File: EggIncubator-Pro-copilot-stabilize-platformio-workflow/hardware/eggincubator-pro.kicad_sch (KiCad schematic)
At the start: 33 parts, among them J1 ESP32 DevKit breakout, J10 ESP32 DevKit 5V / VIN input, J2 SHT31 module, I2C 0x44, J3 DS18B20, 1-Wire, J4 4 optocoupled relay-control o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, J5 BTS7960 module / motor (separ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, J6 Door and turner limit switches, J7 5V buzzer module, Q1 low-side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, J8 Expansion: I2C / ADC sensors, J9 12V DC input, Q1 PN2222A, U1 PC817, U2 PC817, U3 PC817, U4 PC817, U9 12V to 5V buck module

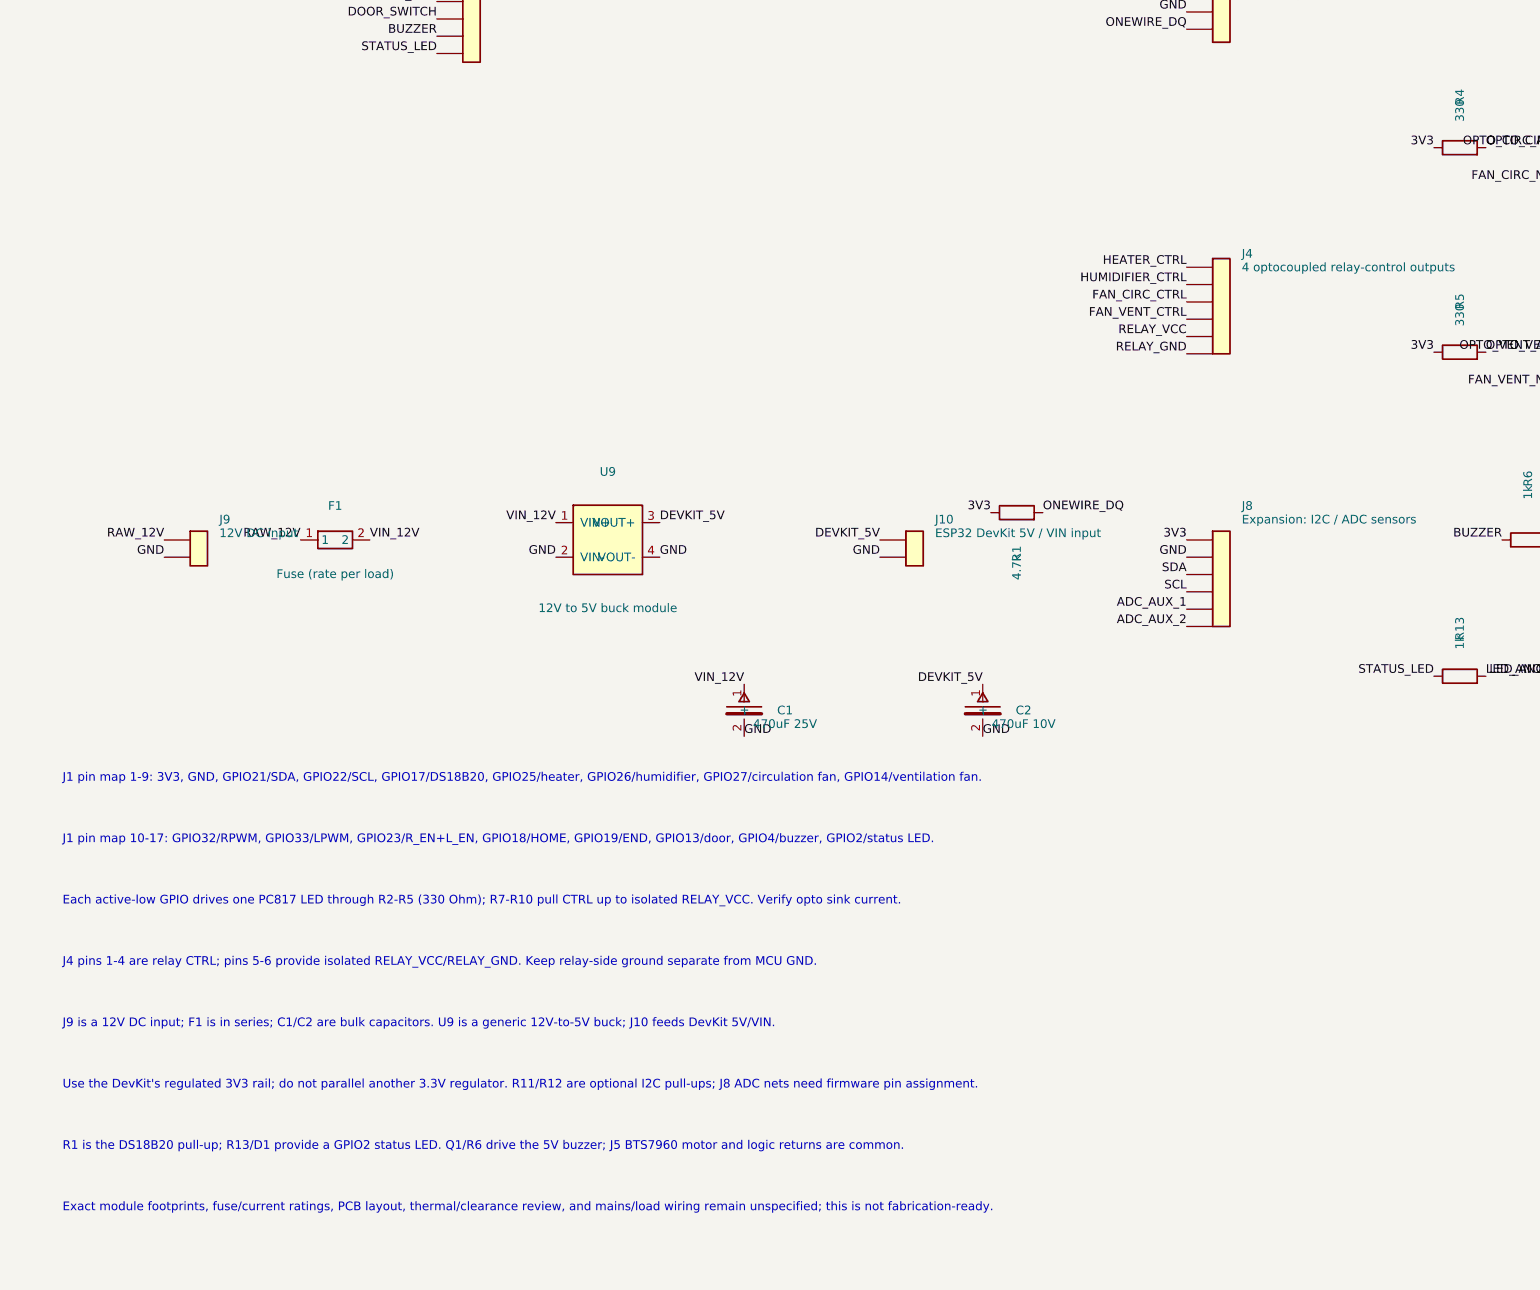
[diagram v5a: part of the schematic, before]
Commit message: Add fused motor power to schematic
Co-authored-by: tomnyle <175001228+tomnyle@users.noreply.github.com>
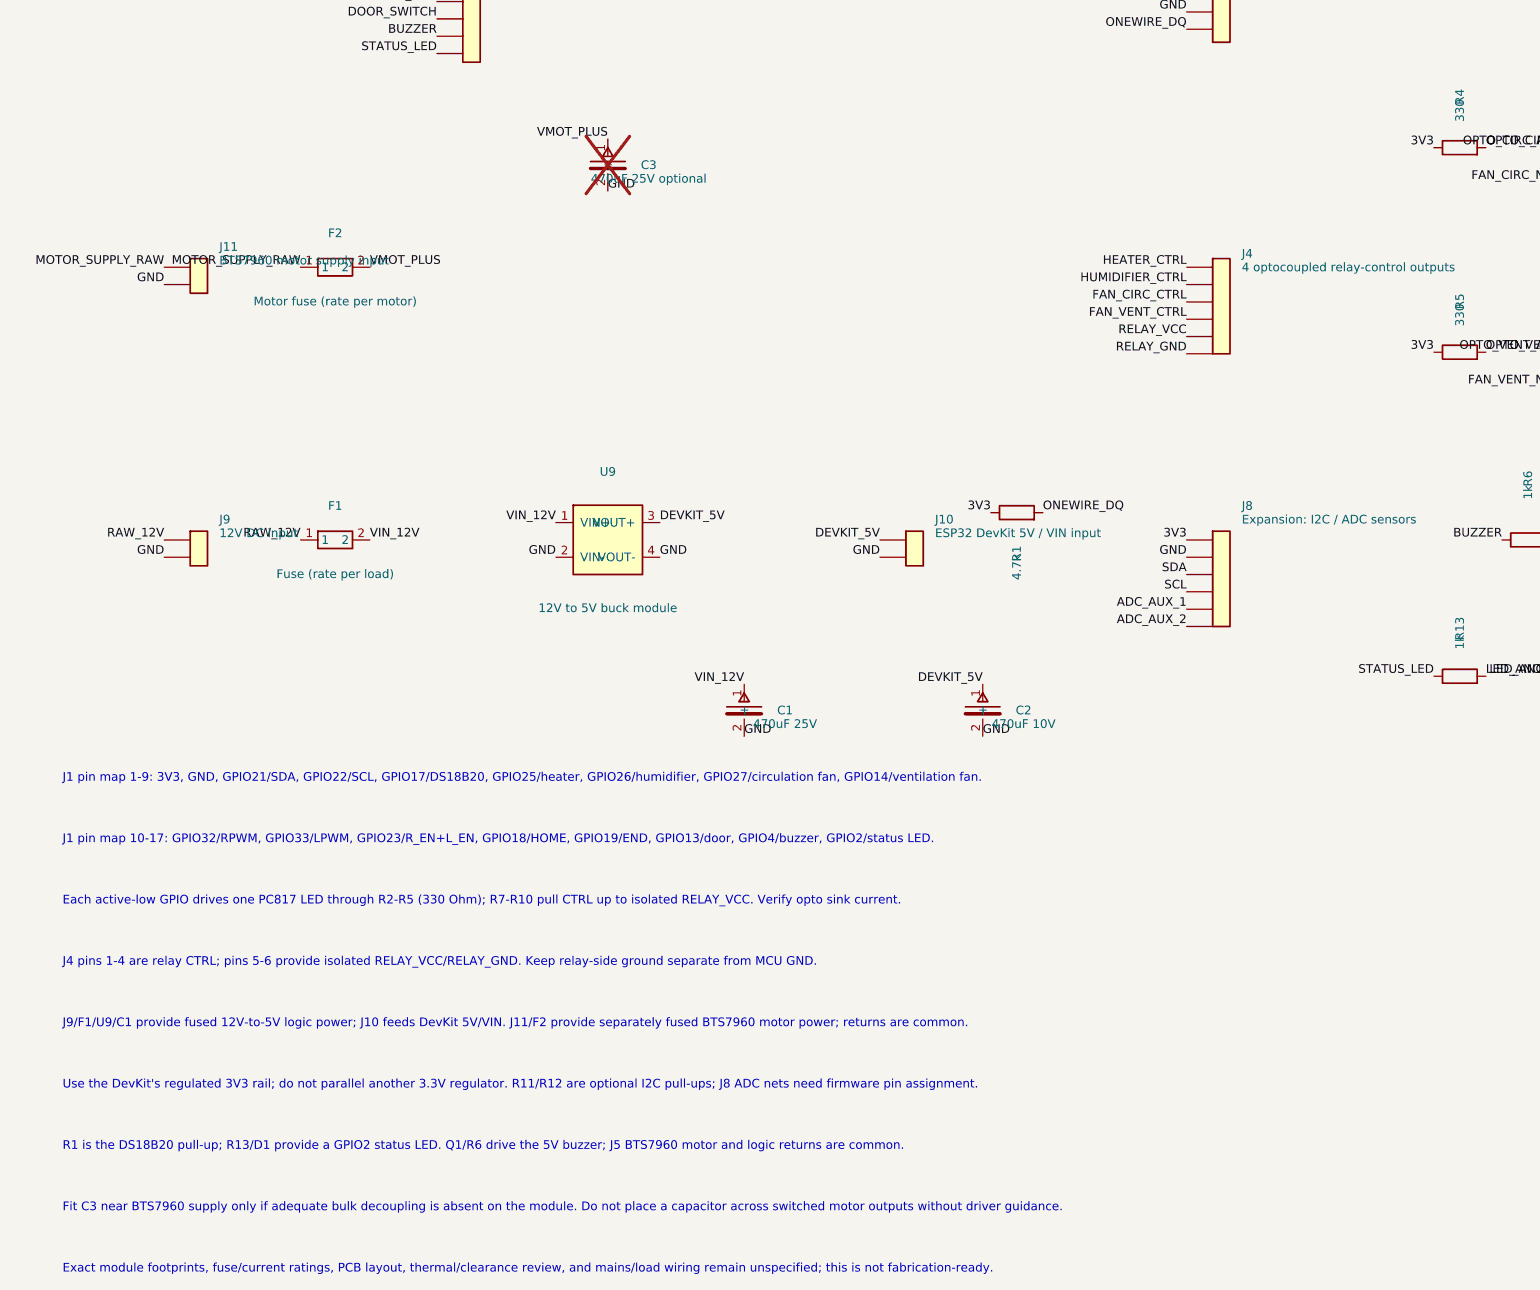
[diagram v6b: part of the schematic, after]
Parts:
- added C3: 470uF 25V optional, symbol EggIncubator:CP
- added F2: Motor fuse (rate per motor), symbol EggIncubator:Fuse
- added J11: BTS7960 motor supply input, symbol Connector_Generic:Conn_01x02
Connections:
- net GND: now also C3.2 (-), J11.2
- net VMOT_PLUS: now also C3.1 (+), F2.2
- new net MOTOR_SUPPLY_RAW: F2.1, J11.1
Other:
- note added: "Fit C3 near BTS7960 supply only if adequate bulk decoupling is absent on the module. Do not place a capacitor across switched motor outputs without driver guidance."
- note added: "J9/F1/U9/C1 provide fused 12V-to-5V logic power; J10 feeds DevKit 5V/VIN. J11/F2 provide separately fused BTS7960 motor power; returns are common."
- note removed: "J9 is a 12V DC input; F1 is in series; C1/C2 are bulk capacitors. U9 is a generic 12V-to-5V buck; J10 feeds DevKit 5V/VIN."
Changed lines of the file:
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@@
     (instances (project "EggIncubator-Pro" (path "/60845d38-2cd0-4dd2-9a8c-c6c7c694e4e9/00000000-0000-4000-8000-000000000055" (reference "J10") (unit 1))))
+  )
+  (symbol (lib_id "Connector_Generic:Conn_01x02") (at 65 130 0) (unit 1) (in_bom yes) (on_board yes) (dnp no)
+    (property "Reference" "J11" (at 68 127 0) (effects (font (size 1.27 1.27)) (justify left)))
+    (property "Value" "BTS7960 motor supply input" (at 68 129 0) (effects (font (size 1.27 1.27)) (justify left)))
+    (property "Footprint" "" (at 65 130 0) (effects (font (size 1.27 1.27)) hide))
+    (property "Datasheet" "~" (at 65 130 0) (effects (font (size 1.27 1.27)) hide))
+    (pin "1") (pin "2")
+    (instances (project "EggIncubator-Pro" (path "/60845d38-2cd0-4dd2-9a8c-c6c7c694e4e9/00000000-0000-4000-8000-000000000172" (reference "J11") (unit 1))))
+  )
+  (symbol (lib_id "EggIncubator:Fuse") (at 85 130 0) (unit 1) (in_bom yes) (on_board yes) (dnp no)
+    (property "Reference" "F2" (at 85 125 0) (effects (font (size 1.27 1.27))))
+    (property "Value" "Motor fuse (rate per motor)" (at 85 135 0) (effects (font (size 1.27 1.27))))
+    (property "Footprint" "" (at 85 130 0) (effects (font (size 1.27 1.27)) hide))
+    (property "Datasheet" "~" (at 85 130 0) (effects (font (size 1.27 1.27)) hide))
+    (pin "1") (pin "2")
+    (instances (project "EggIncubator-Pro" (path "/60845d38-2cd0-4dd2-9a8c-c6c7c694e4e9/00000000-0000-4000-8000-000000000159" (reference "F2") (unit 1))))
+  )
+  (symbol (lib_id "EggIncubator:CP") (at 125 115 0) (unit 1) (in_bom yes) (on_board yes) (dnp yes)
+    (property "Reference" "C3" (at 131 115 0) (effects (font (size 1.27 1.27))))
+    (property "Value" "470uF 25V optional" (at 131 117 0) (effects (font (size 1.27 1.27))))
+    (property "Footprint" "" (at 125 115 0) (effects (font (size 1.27 1.27)) hide))
+    (property "Datasheet" "~" (at 125 115 0) (effects (font (size 1.27 1.27)) hide))
+    (pin "1") (pin "2")
+    (instances (project "EggIncubator-Pro" (path "/60845d38-2cd0-4dd2-9a8c-c6c7c694e4e9/00000000-0000-4000-8000-000000000162" (reference "C3") (unit 1))))
   )
   (symbol (lib_id "EggIncubator:Fuse") (at 85 170 0) (unit 1) (in_bom yes) (on_board yes) (dnp no)
@@
   (label "LED_ANODE" (at 264.92 190 180) (fields_autoplaced) (effects (font (size 1.27 1.27)) (justify right bottom)))
   (label "GND" (at 275.08 190 0) (fields_autoplaced) (effects (font (size 1.27 1.27)) (justify left bottom)))
+  (label "MOTOR_SUPPLY_RAW" (at 59.92 130 180) (fields_autoplaced) (effects (font (size 1.27 1.27)) (justify right bottom)))
+  (label "MOTOR_SUPPLY_RAW" (at 79.92 130 180) (fields_autoplaced) (effects (font (size 1.27 1.27)) (justify right bottom)))
+  (label "VMOT_PLUS" (at 90.08 130 0) (fields_autoplaced) (effects (font (size 1.27 1.27)) (justify left bottom)))
+  (label "GND" (at 59.92 132.54 180) (fields_autoplaced) (effects (font (size 1.27 1.27)) (justify right bottom)))
+  (label "VMOT_PLUS" (at 125 111.19 180) (fields_autoplaced) (effects (font (size 1.27 1.27)) (justify right bottom)))
+  (label "GND" (at 125 118.81 0) (fields_autoplaced) (effects (font (size 1.27 1.27)) (justify left bottom)))
   (text "J1 pin map 1-9: 3V3, GND, GPIO21/SDA, GPIO22/SCL, GPIO17/DS18B20, GPIO25/heater, GPIO26/humidifier, GPIO27/circulation fan, GPIO14/ventilation fan." (at 45 205 0) (effects (font (size 1.27 1.27)) (justify left)))
   (text "J1 pin map 10-17: GPIO32/RPWM, GPIO33/LPWM, GPIO23/R_EN+L_EN, GPIO18/HOME, GPIO19/END, GPIO13/door, GPIO4/buzzer, GPIO2/status LED." (at 45 214 0) (effects (font (size 1.27 1.27)) (justify left)))
   (text "Each active-low GPIO drives one PC817 LED through R2-R5 (330 Ohm); R7-R10 pull CTRL up to isolated RELAY_VCC. Verify opto sink current." (at 45 223 0) (effects (font (size 1.27 1.27)) (justify left)))
   (text "J4 pins 1-4 are relay CTRL; pins 5-6 provide isolated RELAY_VCC/RELAY_GND. Keep relay-side ground separate from MCU GND." (at 45 232 0) (effects (font (size 1.27 1.27)) (justify left)))
-  (text "J9 is a 12V DC input; F1 is in series; C1/C2 are bulk capacitors. U9 is a generic 12V-to-5V buck; J10 feeds DevKit 5V/VIN." (at 45 241 0) (effects (font (size 1.27 1.27)) (justify left)))
+  (text "J9/F1/U9/C1 provide fused 12V-to-5V logic power; J10 feeds DevKit 5V/VIN. J11/F2 provide separately fused BTS7960 motor power; returns are common." (at 45 241 0) (effects (font (size 1.27 1.27)) (justify left)))
   (text "Use the DevKit's regulated 3V3 rail; do not parallel another 3.3V regulator. R11/R12 are optional I2C pull-ups; J8 ADC nets need firmware pin assignment." (at 45 250 0) (effects (font (size 1.27 1.27)) (justify left)))
   (text "R1 is the DS18B20 pull-up; R13/D1 provide a GPIO2 status LED. Q1/R6 drive the 5V buzzer; J5 BTS7960 motor and logic returns are common." (at 45 259 0) (effects (font (size 1.27 1.27)) (justify left)))
-  (text "Exact module footprints, fuse/current ratings, PCB layout, thermal/clearance review, and mains/load wiring remain unspecified; this is not fabrication-ready." (at 45 268 0) (effects (font (size 1.27 1.27)) (justify left)))
+  (text "Fit C3 near BTS7960 supply only if adequate bulk decoupling is absent on the module. Do not place a capacitor across switched motor outputs without driver guidance." (at 45 268 0) (effects (font (size 1.27 1.27)) (justify left)))
+  (text "Exact module footprints, fuse/current ratings, PCB layout, thermal/clearance review, and mains/load wiring remain unspecified; this is not fabrication-ready." (at 45 277 0) (effects (font (size 1.27 1.27)) (justify left)))
   (sheet_instances (path "/" (page "1")))
 )
